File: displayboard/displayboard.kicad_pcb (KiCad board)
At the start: 2 copper layers, 103 x 41 mm, 29 parts, among them P1 CONN_01X08, P2 CONN_01X08, U1 SG-636PCE, U2 LEDM, U3 MAX6960, U4 LEDM, U5 MAX6960, U6 LEDM

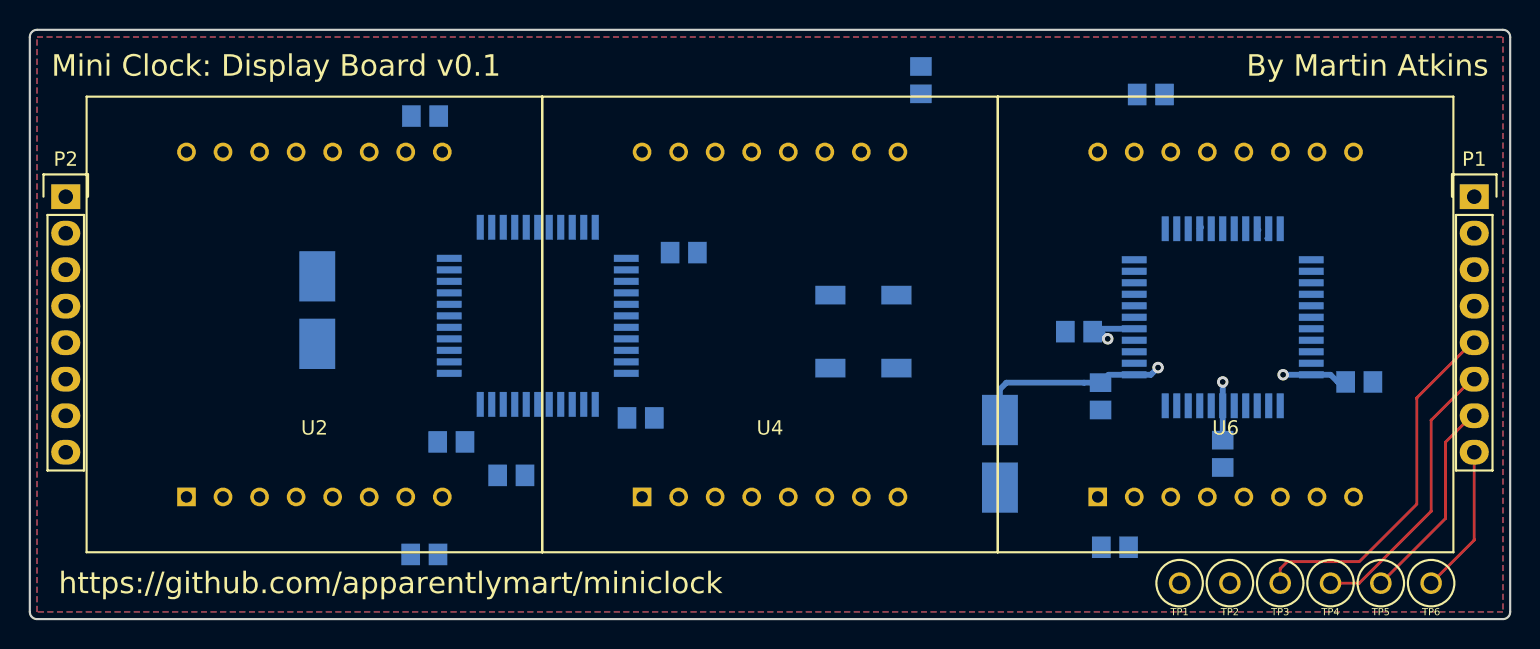
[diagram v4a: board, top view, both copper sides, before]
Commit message: Another attempt at PCB traces.
This became kinda spaghetti-like but I think it should be okay since none
of these signals are high-frequency. The power planes got a bit abused for
some signal routing but hopefully not too much.
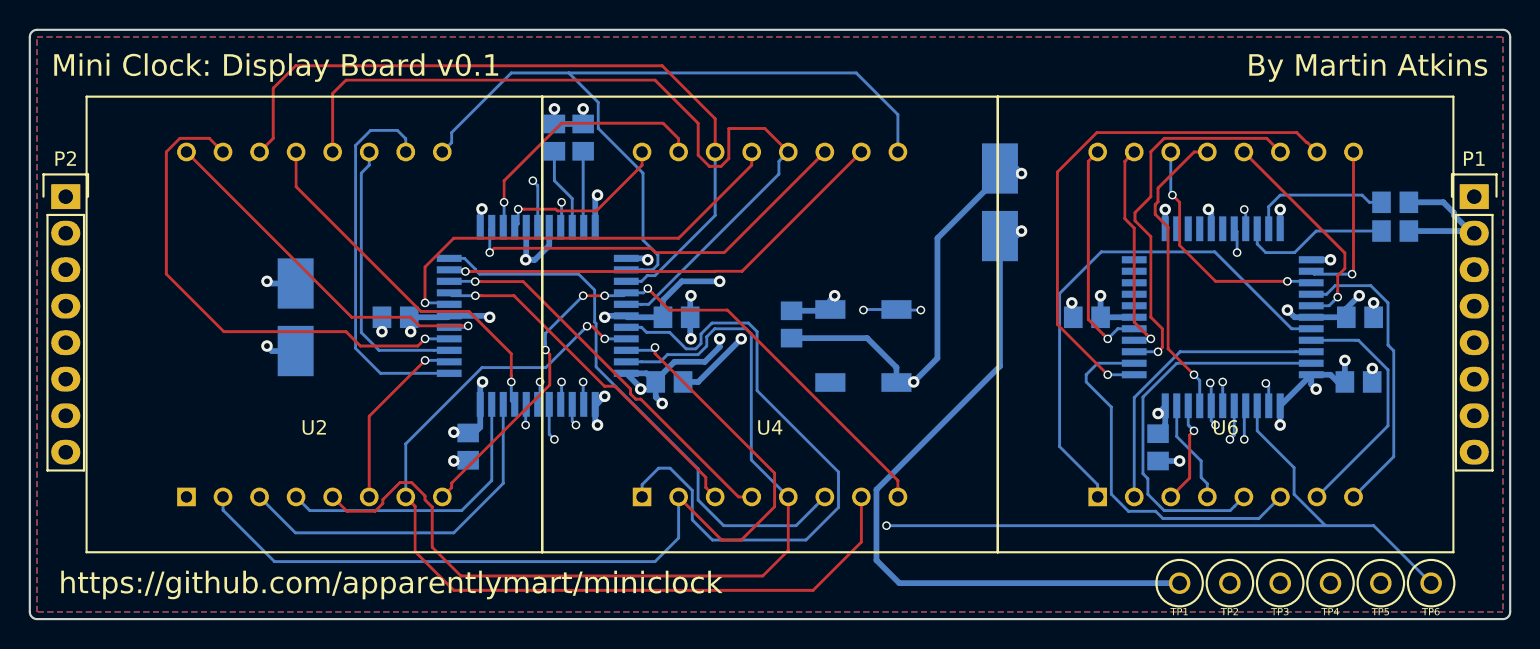
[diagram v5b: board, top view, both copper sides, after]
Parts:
- moved JP1 30.4 mm to (-15.0, -13.0), turned to 270 degrees
- moved JP3 29.4 mm to (43.5, -6.50)
- moved C4 20.5 mm to (-26.1, -0.50), turned to 180 degrees
- moved C1 19.2 mm to (1.50, 0.00)
- moved JP4 18.6 mm to (43.5, -8.50)
- moved C11 17.5 mm to (16.0, -8.50)
- moved C3 15.9 mm to (-6.50, -0.50), turned to 180 degrees
- moved C10 13.5 mm to (41.0, -0.50), turned to 180 degrees
- moved JP2 11.1 mm to (-13.0, -13.0), turned to 90 degrees
- moved C8 5.35 mm to (27.0, 8.55)
- moved C5 3.20 mm to (-7.00, 4.00), turned to 180 degrees
- moved C6 1.58 mm to (-33.0, -0.50), turned to 180 degrees
- moved C2 1.22 mm to (-21.0, 8.50), turned to 270 degrees
- moved C9 1.14 mm to (22.1, -0.50)
- moved U1 1.00 mm to (6.50, 1.50)
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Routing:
- net GND: track 0.00 -> 135.7 mm, vias 0 -> 25
- net ~RESET: track 0.15 -> 85.9 mm, vias 0 -> 3
- net SSEL: track 10.5 -> 91.9 mm, vias 0 -> 2
- net D0_R5: track 0.00 -> 79.2 mm
- net MISO: track 14.4 -> 87.4 mm, vias 0 -> 2
- net MOSI: track 19.6 -> 89.9 mm, vias 0 -> 2
- net SCLK: track 25.5 -> 94.7 mm, vias 0 -> 2
- net Net-(U3-Pad39): track 0.00 -> 66.1 mm, vias 0 -> 2
- net D0_R8: track 0.00 -> 64.6 mm
- net D0_R6: track 0.00 -> 63.6 mm, vias 0 -> 2
- net D0_R7: track 0.00 -> 63.1 mm, vias 0 -> 1
- net D0_R4: track 0.00 -> 59.1 mm
- net ADDCLK: track 0.00 -> 57.6 mm, vias 0 -> 2
- net D0_R1: track 0.00 -> 56.4 mm
- net OSC: track 0.00 -> 55.8 mm, vias 0 -> 4
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- added copper zone on B.Cu, net +3V3
- added copper zone on VCC, net +3V3
- added copper zone on F.Cu, net GND
- added copper zone on GND, net GND
- removed copper zone on F.Cu, net +3V3
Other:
- copper layers 2 -> 4

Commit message: 3D models of some of the components.
Also flipped the inter-board connection headers since they were on the
wrong side of the board as far as KiCad is concerned.
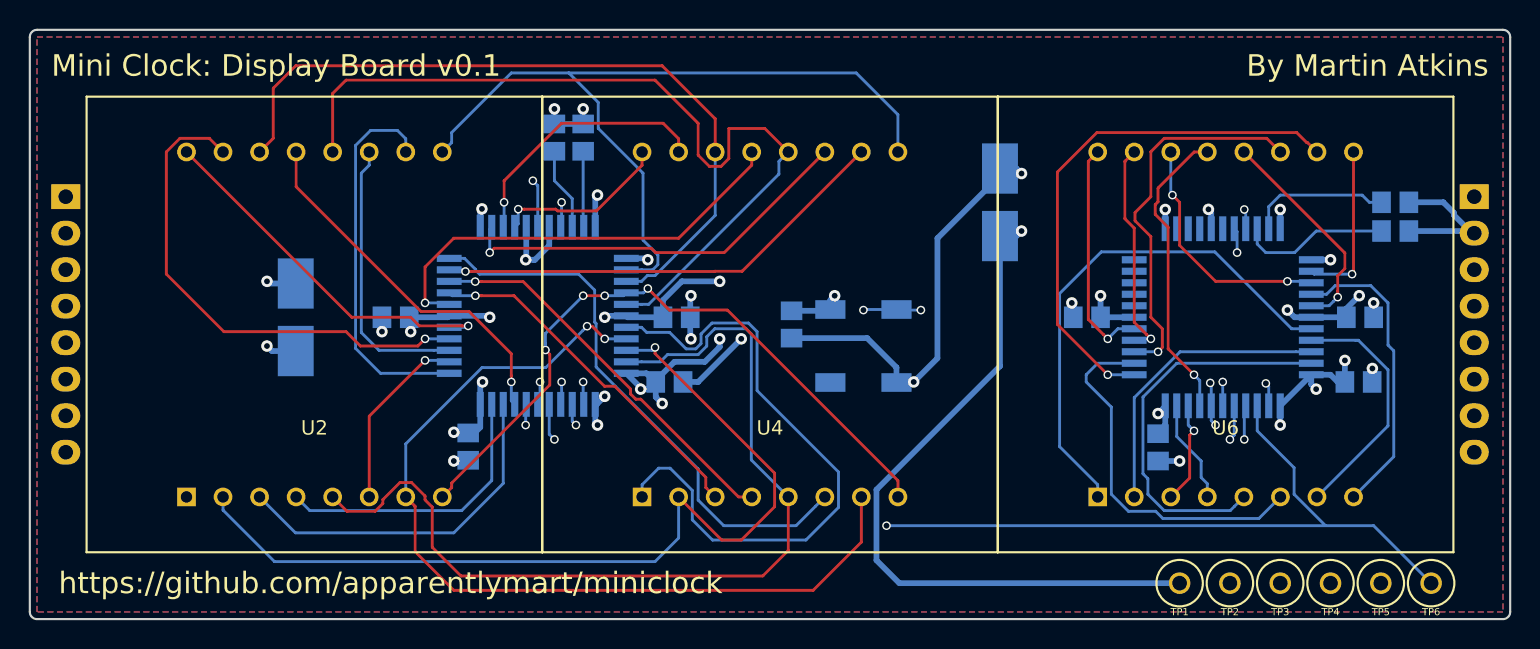
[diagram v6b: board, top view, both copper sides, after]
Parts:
- P1, P2: moved to B.Cu
- turned P1 to 180 degrees
- turned P2 to 180 degrees

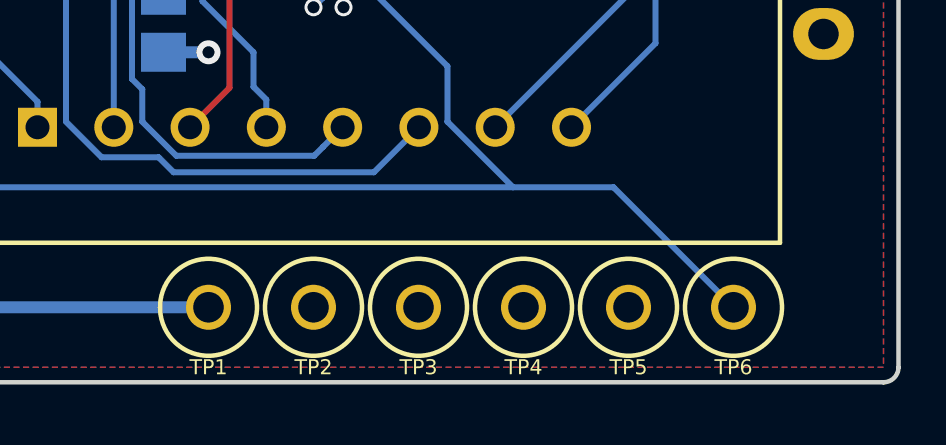
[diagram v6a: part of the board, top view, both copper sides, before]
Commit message: Label the test points.
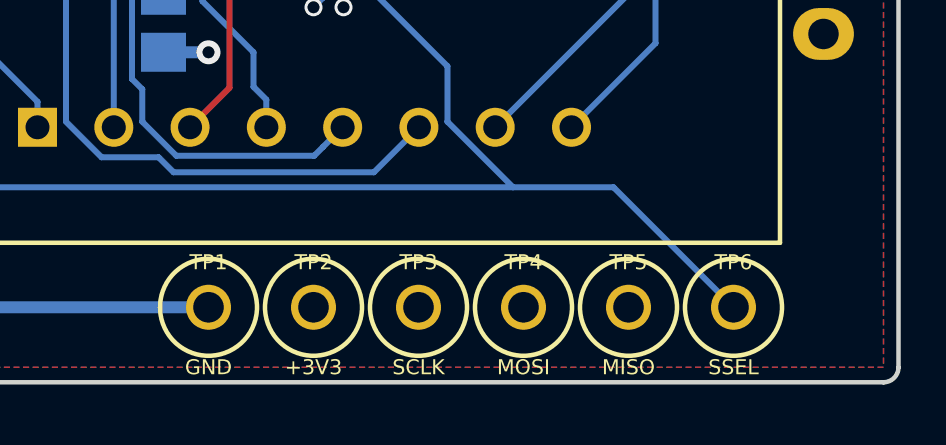
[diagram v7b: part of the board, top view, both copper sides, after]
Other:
- board text added: "+3V3"
- board text added: "GND"
- board text added: "MISO"
- board text added: "MOSI"
- board text added: "SCLK"
- board text added: "SSEL"
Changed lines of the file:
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@@
     (area -51.575001 -20.575001 51.575001 20.575001)
     (thickness 1.6)
-    (drawings 11)
+    (drawings 17)
     (tracks 776)
     (zones 0)
@@
   (module miniclock:TESTPOINT (layer F.Cu)
     (at 28.5 18)
-    (fp_text reference TP1 (at 0 2) (layer F.SilkS)
+    (fp_text reference TP1 (at 0 -1.5) (layer F.SilkS)
       (effects (font (size 0.5 0.5) (thickness 0.1)))
     )
@@
   (module miniclock:TESTPOINT (layer F.Cu)
     (at 32 18)
-    (fp_text reference TP2 (at 0 2) (layer F.SilkS)
+    (fp_text reference TP2 (at 0 -1.5) (layer F.SilkS)
       (effects (font (size 0.5 0.5) (thickness 0.1)))
     )
@@
   (module miniclock:TESTPOINT (layer F.Cu)
     (at 35.5 18)
-    (fp_text reference TP3 (at 0 2) (layer F.SilkS)
+    (fp_text reference TP3 (at 0 -1.5) (layer F.SilkS)
       (effects (font (size 0.5 0.5) (thickness 0.1)))
     )
@@
   (module miniclock:TESTPOINT (layer F.Cu)
     (at 39 18)
-    (fp_text reference TP4 (at 0 2) (layer F.SilkS)
+    (fp_text reference TP4 (at 0 -1.5) (layer F.SilkS)
       (effects (font (size 0.5 0.5) (thickness 0.1)))
     )
@@
   (module miniclock:TESTPOINT (layer F.Cu)
     (at 42.5 18)
-    (fp_text reference TP5 (at 0 2) (layer F.SilkS)
+    (fp_text reference TP5 (at 0 -1.5) (layer F.SilkS)
       (effects (font (size 0.5 0.5) (thickness 0.1)))
     )
@@
   (module miniclock:TESTPOINT (layer F.Cu)
     (at 46 18)
-    (fp_text reference TP6 (at 0 2) (layer F.SilkS)
+    (fp_text reference TP6 (at 0 -1.5) (layer F.SilkS)
       (effects (font (size 0.5 0.5) (thickness 0.1)))
     )
@@
     )
   )
+  (gr_text SSEL (at 46 20) (layer F.SilkS)
+    (effects (font (size 0.5 0.5) (thickness 0.125)))
+  )
+  (gr_text MISO (at 42.5 20) (layer F.SilkS)
+    (effects (font (size 0.5 0.5) (thickness 0.125)))
+  )
+  (gr_text MOSI (at 39 20) (layer F.SilkS)
+    (effects (font (size 0.5 0.5) (thickness 0.125)))
+  )
+  (gr_text SCLK (at 35.5 20) (layer F.SilkS)
+    (effects (font (size 0.5 0.5) (thickness 0.125)))
+  )
+  (gr_text +3V3 (at 32 20) (layer F.SilkS)
+    (effects (font (size 0.5 0.5) (thickness 0.125)))
+  )
+  (gr_text GND (at 28.5 20) (layer F.SilkS)
+    (effects (font (size 0.5 0.5) (thickness 0.125)))
+  )
   (gr_text https://github.com/apparentlymart/miniclock (at -49.5 18) (layer F.SilkS)
